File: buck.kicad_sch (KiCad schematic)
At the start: 11 parts, among them IC3 LM5085MY_NOPB, Q3 PMOS

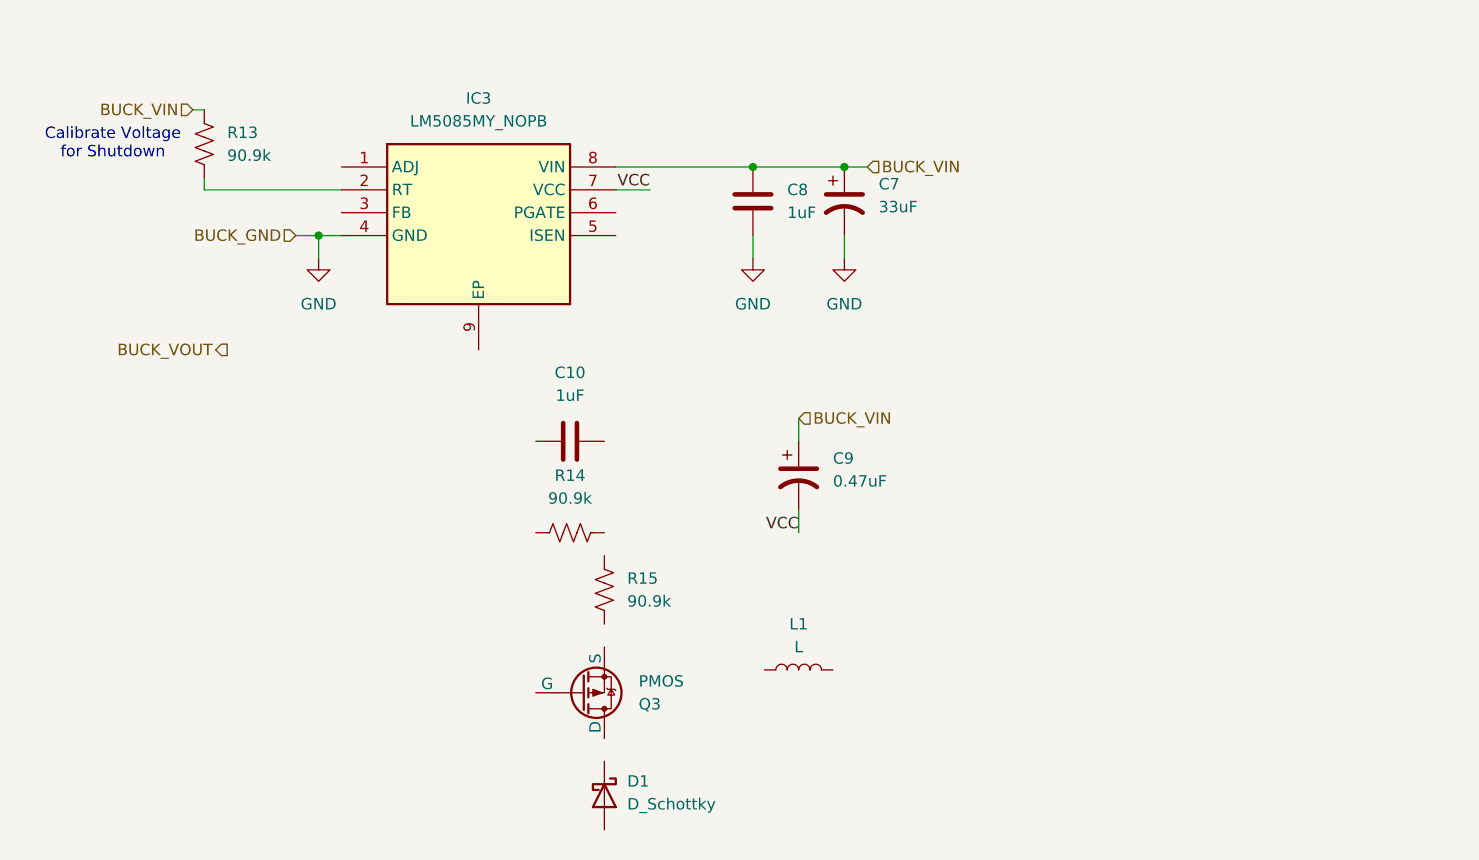
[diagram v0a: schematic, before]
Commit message: added LDO and fixed connections in power
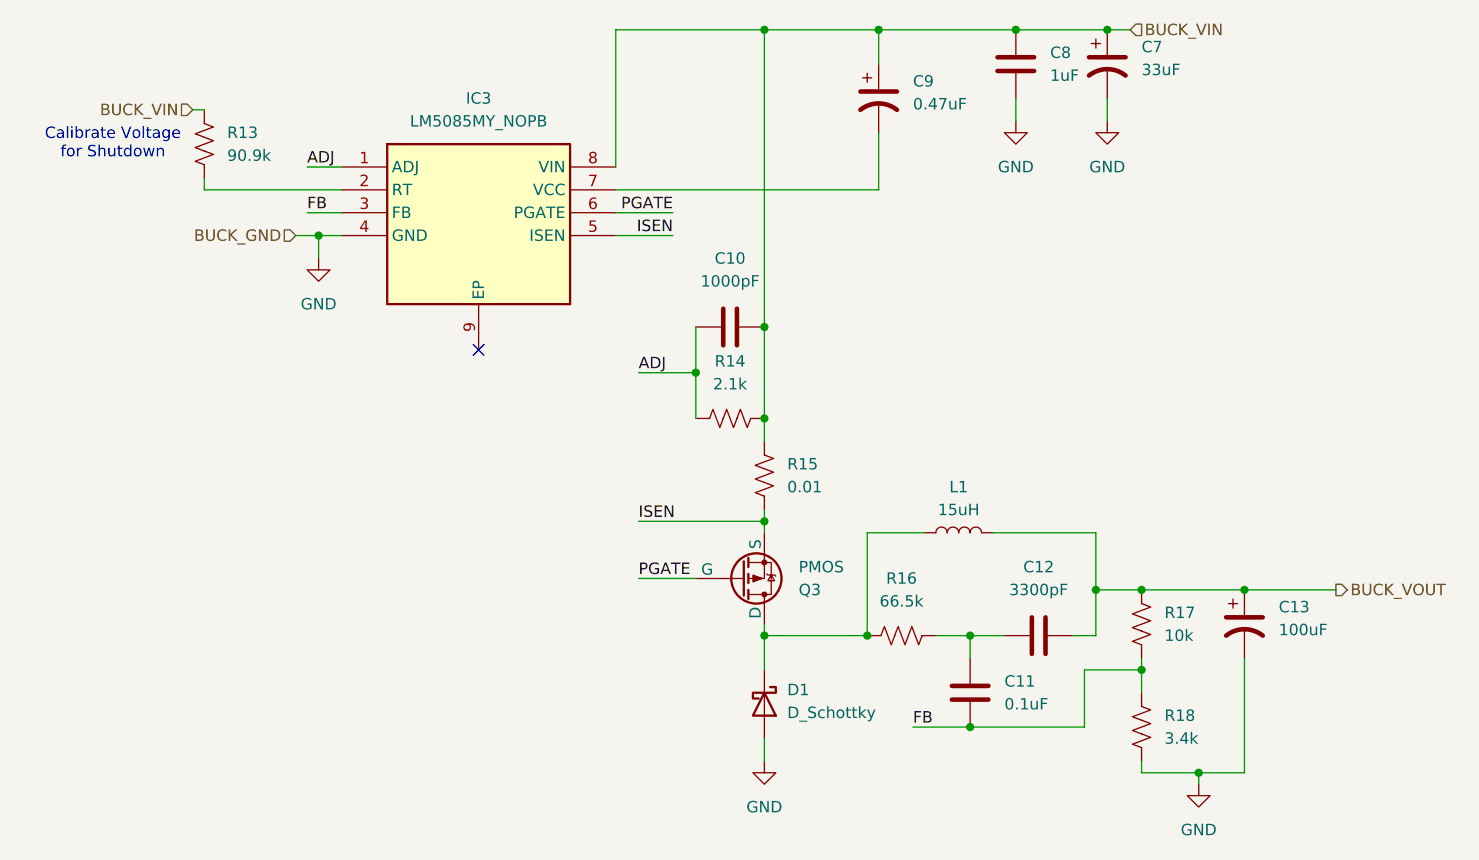
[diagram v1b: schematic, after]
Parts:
- added C11: 0.1uF, symbol Device:C
- added C12: 3300pF, symbol Device:C
- added C13: 100uF, symbol Device:C_Polarized_US
- added R16: 66.5k, symbol Device:R_US
- added R17: 10k, symbol Device:R_US
- added R18: 3.4k, symbol Device:R_US
- C10: value 1uF -> 1000pF
- L1: value L -> 15uH
- R14: value 90.9k -> 2.1k
- R15: value 90.9k -> 0.01
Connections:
- net BUCK_VIN: now also C10.2, R14.2, R15.1
- net BUCK_VOUT: now also L1.2, C12.2, C13.1, R17.1
- net GND: now also D1.2 (A), C13.2, R18.2
- net ADJ: now reaches C10.1
- net ADJ: now also IC3.1 (ADJ), R14.1
- net at Q3.1 (D): now also D1.1 (K), L1.1, R16.2
- net PGATE: now reaches Q3.2 (G)
- net PGATE: now also IC3.6 (PGATE)
- net ISEN: now reaches Q3.3 (S)
- net ISEN: now also IC3.5 (ISEN), R15.2
- net FB: now reaches IC3.3 (FB)
- net FB: now also C11.2, R17.2, R18.1
- net VCC: no longer names the net of C9.2, IC3.7 (VCC)
- new net: C11.1, C12.1, R16.1
- no-connect marks 0 -> 1
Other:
- moved on the sheet: C10, C7, C8, D1, L1, Q3, R14, R15
